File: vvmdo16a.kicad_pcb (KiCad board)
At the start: 2 copper layers, 51.8 x 61.5 mm, 18 parts, among them J1 517-N2510-6002RB, J2 517-N2520-6002RB, SW1 SW_Coded_SH-7010, U1 PCA9685PW, U2 ULN2803A, U3 ULN2803A

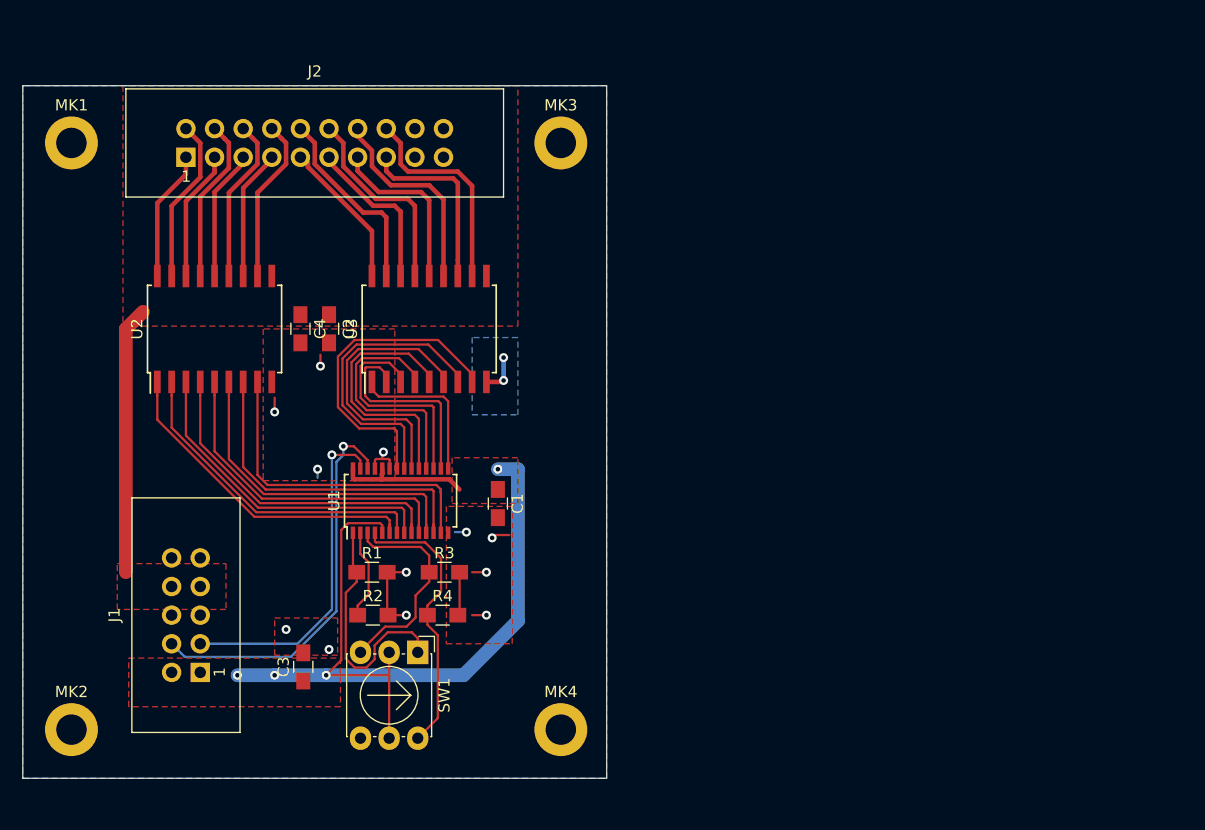
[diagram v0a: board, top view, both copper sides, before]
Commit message: More compact PCB
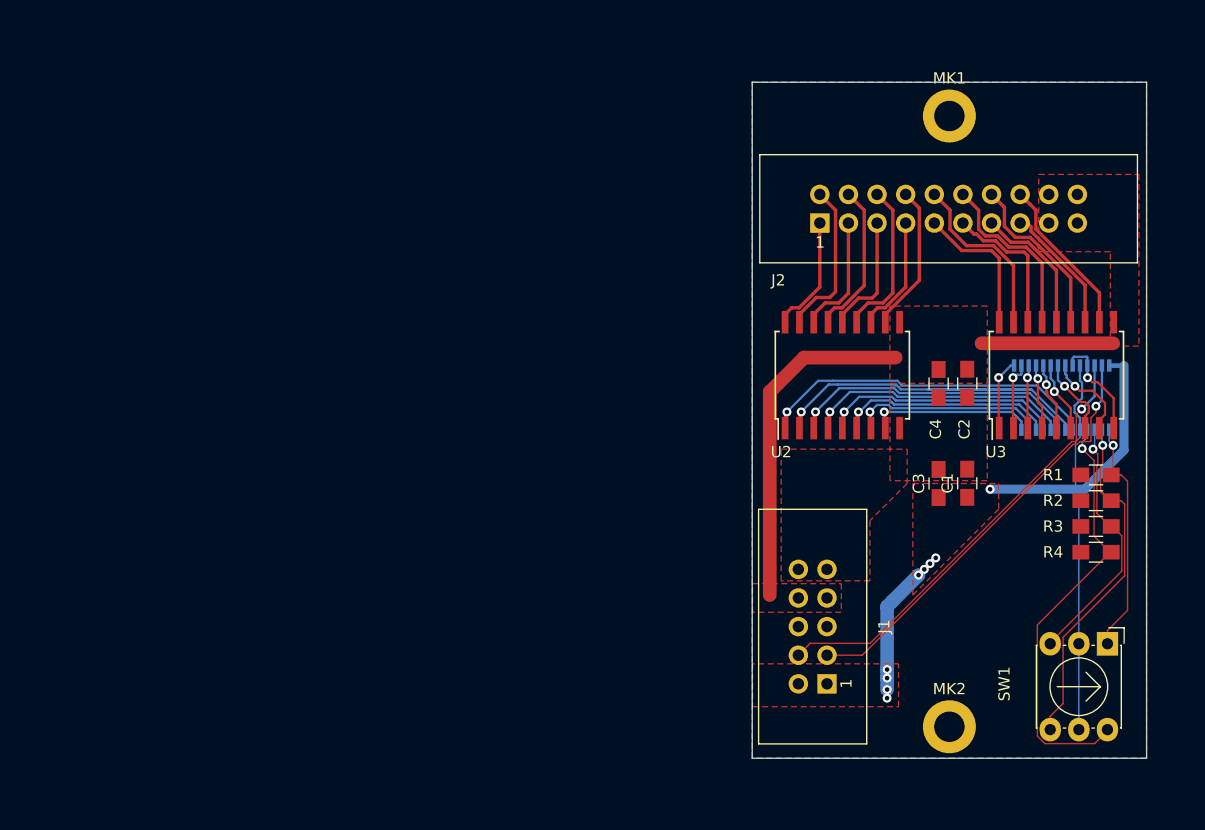
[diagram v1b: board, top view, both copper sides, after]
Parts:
- removed MK3, MK4: Mounting_Hole_PAD, Mounting_Holes:MountingHole_2.7mm_M2.5_DIN965_Pad
- MK1, MK2: value Mounting_Hole_PAD -> M2.5
- SW1: value SW_Coded_SH-7010 -> 220ADC16
- U1: moved to B.Cu
- moved MK1 78.0 mm to (146.5, 70.0)
- moved MK2 77.9 mm to (146.5, 124.2)
- moved R2 65.0 mm to (159.5, 104.1), turned to 180 degrees
- moved R1 64.8 mm to (159.5, 101.9), turned to 180 degrees
- moved SW1 61.2 mm to (160.5, 116.8)
- moved U1 59.4 mm to (156.5, 95.0)
- moved C3 58.7 mm to (145.5, 102.6)
- moved R4 58.3 mm to (159.5, 108.7), turned to 180 degrees
- moved R3 58.0 mm to (159.5, 106.4), turned to 180 degrees
- moved C4 56.9 mm to (145.5, 93.7)
- moved C2 56.8 mm to (148.1, 93.7)
- moved J2 56.6 mm to (135.0, 79.5)
- moved U2 55.9 mm to (137.0, 93.0)
- moved U3 55.8 mm to (156.0, 93.0)
- moved J1 55.6 mm to (135.6, 120.4)
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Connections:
- net Net-(R1-Pad1) renamed /A0
- net Net-(R2-Pad1) renamed /A1
- net Net-(R3-Pad1) renamed /A2
- net Net-(R4-Pad1) renamed /A3
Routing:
- net /A1: track 8.02 -> 32.2 mm, vias 0 -> 1
- net /PWM16: track 28.4 -> 7.91 mm, vias 0 -> 1
- net /PWM15: track 26.6 -> 6.78 mm, vias 0 -> 1
- net /PWM14: track 24.8 -> 6.29 mm, vias 0 -> 1
- net +12V: track 23.7 -> 42.2 mm
- net /PWM13: track 23.2 -> 6.03 mm, vias 0 -> 1
- net +3V3: track 85.1 -> 68.8 mm, vias 4 -> 9
- net /PWM12: track 21.5 -> 5.78 mm, vias 0 -> 1
- net /PWM11: track 19.9 -> 5.61 mm, vias 0 -> 1
- net /PWM8: track 28.9 -> 14.7 mm, vias 0 -> 1
- net GND: track 23.5 -> 9.59 mm, vias 11 -> 1
- net /A3: track 25.4 -> 38.2 mm, vias 0 -> 1
- net /PWM7: track 29.8 -> 17.2 mm, vias 0 -> 1
- net /PWM10: track 18.1 -> 6.13 mm, vias 0 -> 1
- net /PWM6: track 29.7 -> 19.2 mm, vias 0 -> 1
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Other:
- board size 51.8 x 61.5 mm -> 35 x 60 mm
- net class Default: clearance 0.2 -> 0.127; trace_width 0.25 -> 0.127
- rule trace_clearance: 0.2 -> 0.127
- rule trace_min: 0.2 -> 0.127

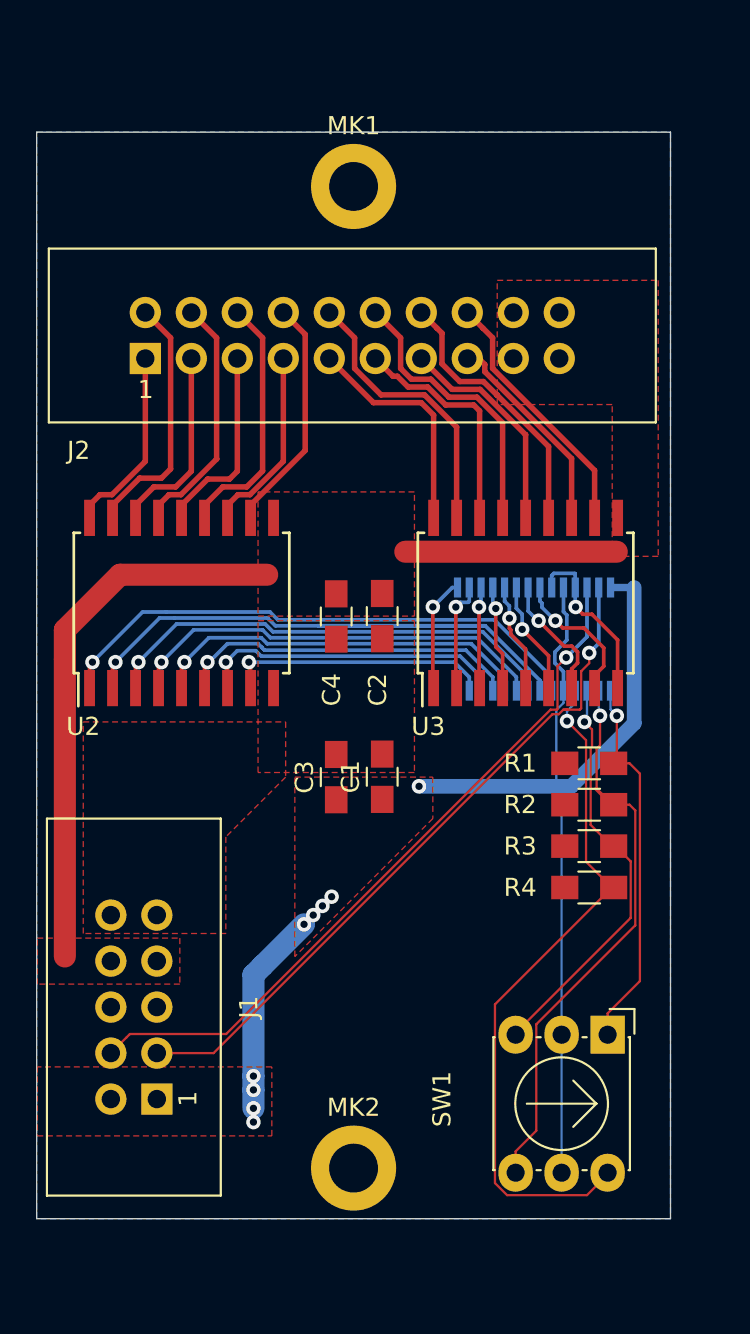
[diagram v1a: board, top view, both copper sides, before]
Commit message: Add seperate power rail input Label the board
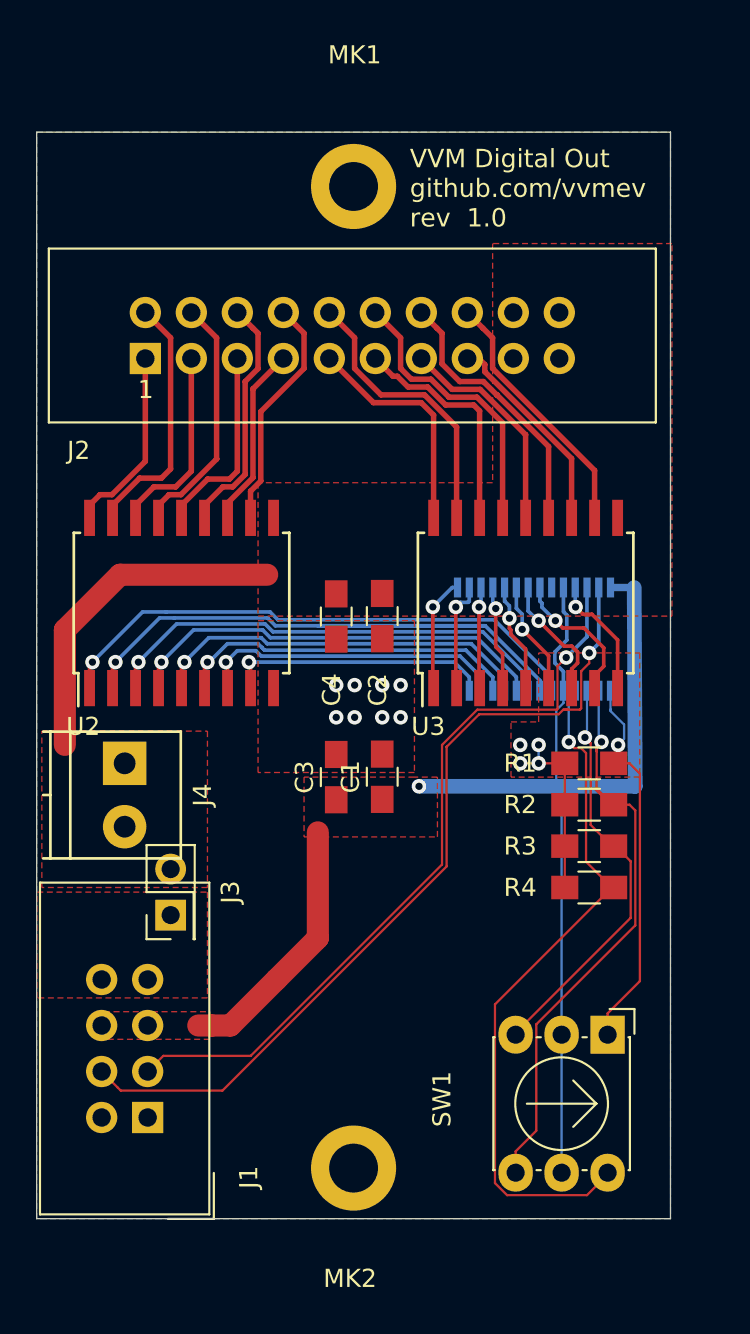
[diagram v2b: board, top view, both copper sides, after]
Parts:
- added J3: Conn_02x01, Pin_Headers:Pin_Header_Straight_2x01_Pitch2.54mm, F.Cu at (136.4, 110.2)
- added J4: Conn_02x01, TerminalBlocks_Phoenix:TerminalBlock_Phoenix_PT-3.5mm_2pol, F.Cu at (133.9, 101.9)
- J1: value 517-N2510-6002RB -> 517-N2508-6002RB; footprint Connectors_IDC:IDC-Header_2x05_Pitch2.54mm_Straight -> Connector-IDC:IDC-Header_2x04_P2.54mm_Vertical
- moved J1 1.14 mm to (135.1, 121.4), turned to 180 degrees
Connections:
- J1 pad 1: +3V3 -> GND
- J1 pad 2: +3V3 -> GND
- J1 pad 3: /SDA -> /SCL
- J1 pad 4: /SCL -> /SDA
- J1 pad 5: Net-(J1-Pad5) -> +3V3
- J1 pad 6: Net-(J1-Pad6) -> +3V3
- J1 pad 7: +12V -> /+12VIN
- J1 pad 8: +12V -> /+12VIN
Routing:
- net +12V: track 42.2 -> 18.8 mm
- net /SDA: track 38.6 -> 46.8 mm
- net GND: track 9.59 -> 17.2 mm, vias 1 -> 13
- net +3V3: track 68.8 -> 71.8 mm, vias 9 -> 1
- net /SCL: track 39.9 -> 42.2 mm
- net /A3: track 38.2 -> 39.1 mm
- net /O6: track 14.0 -> 13.4 mm
- net /O8: track 13.1 -> 13.7 mm
- net /A0: track 21.1 -> 21.6 mm
- added copper zone on F.Cu, net /+12VIN
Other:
- board text added: "VVM Digital Out github.com/vvmev rev 1.0"

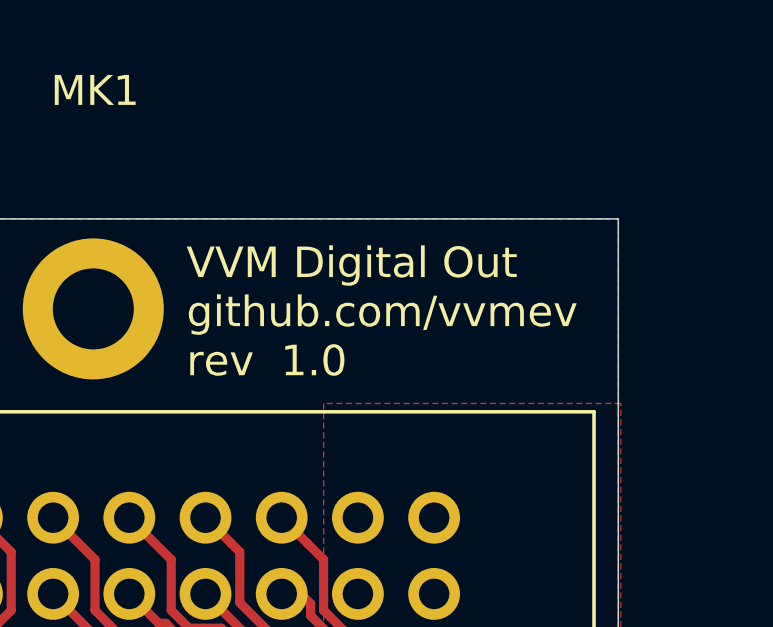
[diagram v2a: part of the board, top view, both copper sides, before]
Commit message: correct board name
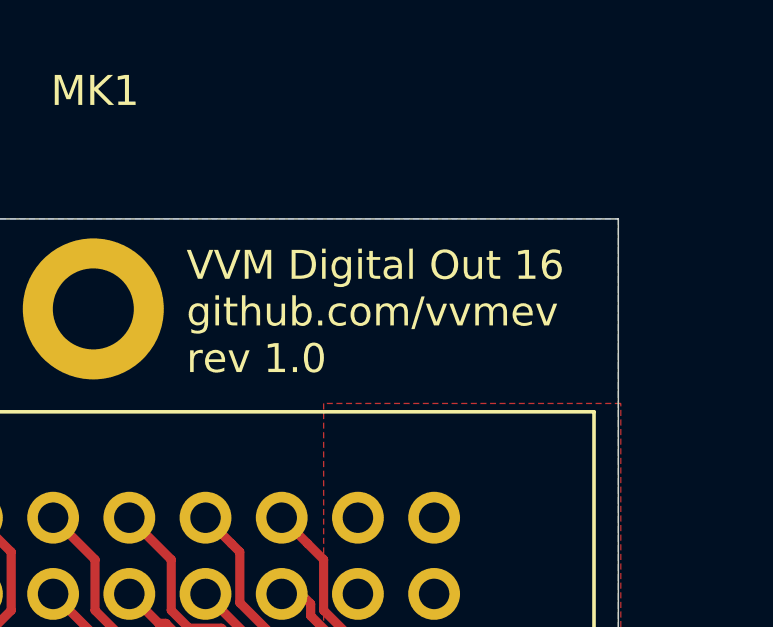
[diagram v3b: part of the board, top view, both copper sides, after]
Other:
- board text added: "VVM Digital Out 16 github.com/vvmev rev 1.0"
- board text removed: "VVM Digital Out github.com/vvmev rev 1.0"
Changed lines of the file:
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@@
   )
   (setup
-    (last_trace_width 1.2192)
+    (last_trace_width 0.127)
     (user_trace_width 0.2032)
     (user_trace_width 0.3048)
@@
     )
   )
-  (gr_text "VVM Digital Out\ngithub.com/vvmev\nrev  1.0" (at 149.606 70.104) (layer F.SilkS)
-    (effects (font (size 1.016 1.016) (thickness 0.1524)) (justify left))
+  (gr_text "VVM Digital Out 16\ngithub.com/vvmev\nrev 1.0" (at 149.606 70.104) (layer F.SilkS)
+    (effects (font (size 0.9652 0.9652) (thickness 0.1524)) (justify left))
   )
   (dimension 35 (width 0.15) (layer Dwgs.User)

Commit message: ready for plotting
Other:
- board text added: "+"
- board text added: "-"
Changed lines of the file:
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@@
   (general
     (thickness 1.6)
-    (drawings 7)
+    (drawings 9)
     (tracks 382)
     (zones 0)
@@
       (outputformat 1)
       (mirror false)
-      (drillshape 1)
+      (drillshape 0)
       (scaleselection 1)
-      (outputdirectory ""))
+      (outputdirectory "gerber"))
   )
   (net 0 "")
@@
     )
   )
+  (gr_text - (at 138.684 105.41 90) (layer F.SilkS)
+    (effects (font (size 1.5 1.5) (thickness 0.3)))
+  )
+  (gr_text + (at 138.684 101.6 90) (layer F.SilkS)
+    (effects (font (size 1.5 1.5) (thickness 0.3)))
+  )
   (gr_text "VVM Digital Out 16\ngithub.com/vvmev\nrev 1.0" (at 149.606 70.104) (layer F.SilkS)
